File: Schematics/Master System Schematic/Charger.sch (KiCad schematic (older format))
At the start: 5 parts

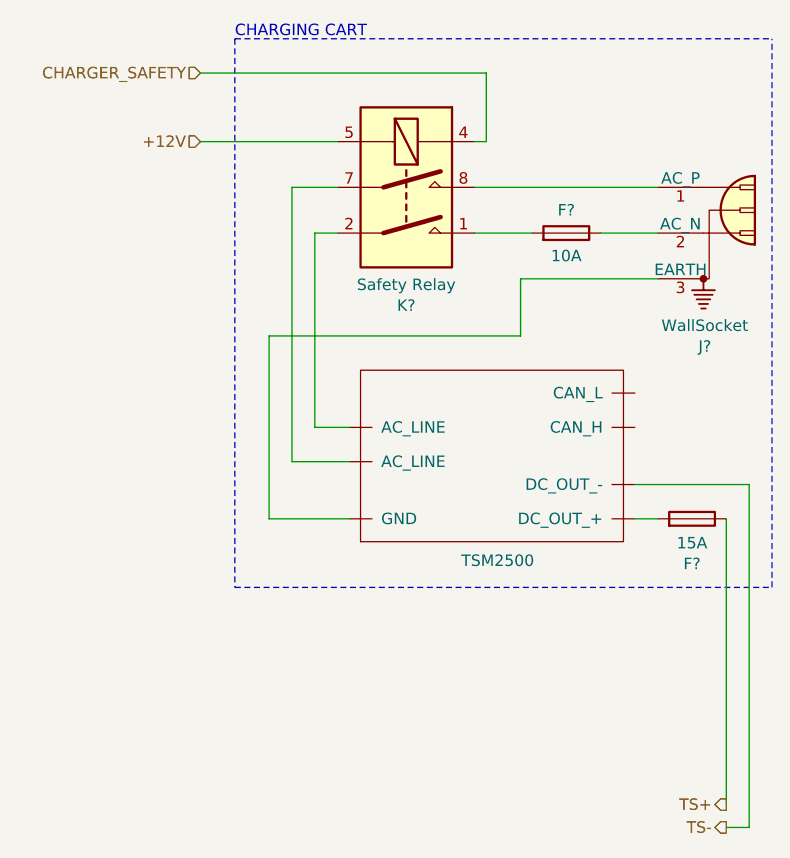
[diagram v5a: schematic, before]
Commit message: Connectors and Start of Numbering
Created new generic connectors and applied numbering tool to whole project
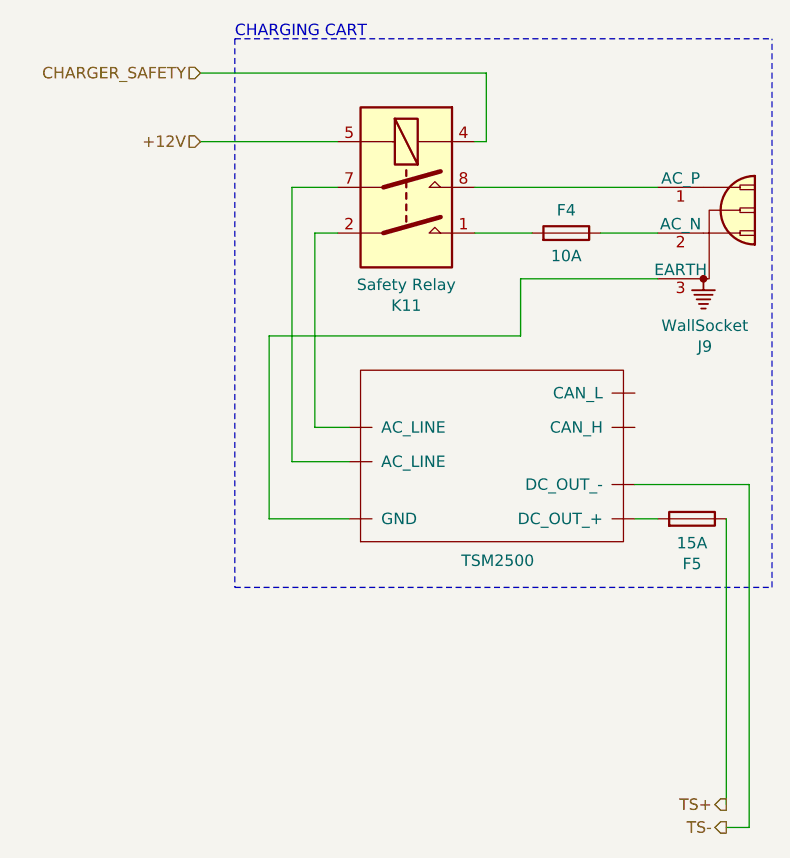
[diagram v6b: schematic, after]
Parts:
- gave numbers to parts that had none: 5
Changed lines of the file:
@@
 EESchema Schematic File Version 4
+LIBS:Master System Schematic-cache
 EELAYER 30 0
 EELAYER END
@@
 P 5200 2750
 AR Path="/61EEF404" Ref="K?"  Part="1"
-AR Path="/61ECC7CF/61EEF404" Ref="K?"  Part="1"
-F 0 "K?" H 5200 2233 50  0000 C CNN
+AR Path="/61ECC7CF/61EEF404" Ref="K11"  Part="1"
+F 0 "K11" H 5200 2233 50  0000 C CNN
 F 1 "Safety Relay" H 5200 2324 50  0000 C CNN
 F 2 "Relay_THT:Relay_DPST_Fujitsu_FTR-F1A" H 5200 2350 50  0001 C CNN
@@
 P 5900 2950
 AR Path="/61EEF40A" Ref="F?"  Part="1"
-AR Path="/61ECC7CF/61EEF40A" Ref="F?"  Part="1"
-F 0 "F?" V 6000 2950 50  0000 C CNN
+AR Path="/61ECC7CF/61EEF40A" Ref="F4"  Part="1"
+F 0 "F4" V 6000 2950 50  0000 C CNN
 F 1 "10A" V 5800 2950 50  0000 C CNN
 F 2 "" V 5830 2950 50  0001 C CNN
@@
 P 5550 4350
 AR Path="/61EEF410" Ref="U?"  Part="1"
-AR Path="/61ECC7CF/61EEF410" Ref="U?"  Part="1"
-F 0 "U?" H 5550 4350 50  0001 C CNN
+AR Path="/61ECC7CF/61EEF410" Ref="U8"  Part="1"
+F 0 "U8" H 5550 4350 50  0001 C CNN
 F 1 "TSM2500" H 5600 4383 50  0000 C CNN
 F 2 "" H 5550 4350 50  0001 C CNN
@@
 P 6450 4200
 AR Path="/61EEF417" Ref="F?"  Part="1"
-AR Path="/61ECC7CF/61EEF417" Ref="F?"  Part="1"
-F 0 "F?" V 6253 4200 50  0000 C CNN
+AR Path="/61ECC7CF/61EEF417" Ref="F5"  Part="1"
+F 0 "F5" V 6253 4200 50  0000 C CNN
 F 1 "15A" V 6344 4200 50  0000 C CNN
 F 2 "" V 6380 4200 50  0001 C CNN
@@
 P 6500 2950
 AR Path="/61EEF421" Ref="J?"  Part="1"
-AR Path="/61ECC7CF/61EEF421" Ref="J?"  Part="1"
-F 0 "J?" H 6506 2454 50  0000 C CNN
+AR Path="/61ECC7CF/61EEF421" Ref="J9"  Part="1"
+F 0 "J9" H 6506 2454 50  0000 C CNN
 F 1 "WallSocket" H 6506 2545 50  0000 C CNN
 F 2 "" H 6200 3050 50  0001 C CNN
